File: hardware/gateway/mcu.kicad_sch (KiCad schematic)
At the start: 23 parts, among them IC1 ATTINY406-MFR, J1 M20-9770342, J2 M20-9770342, Q1 IRLML6402TRPBF, U1 2462

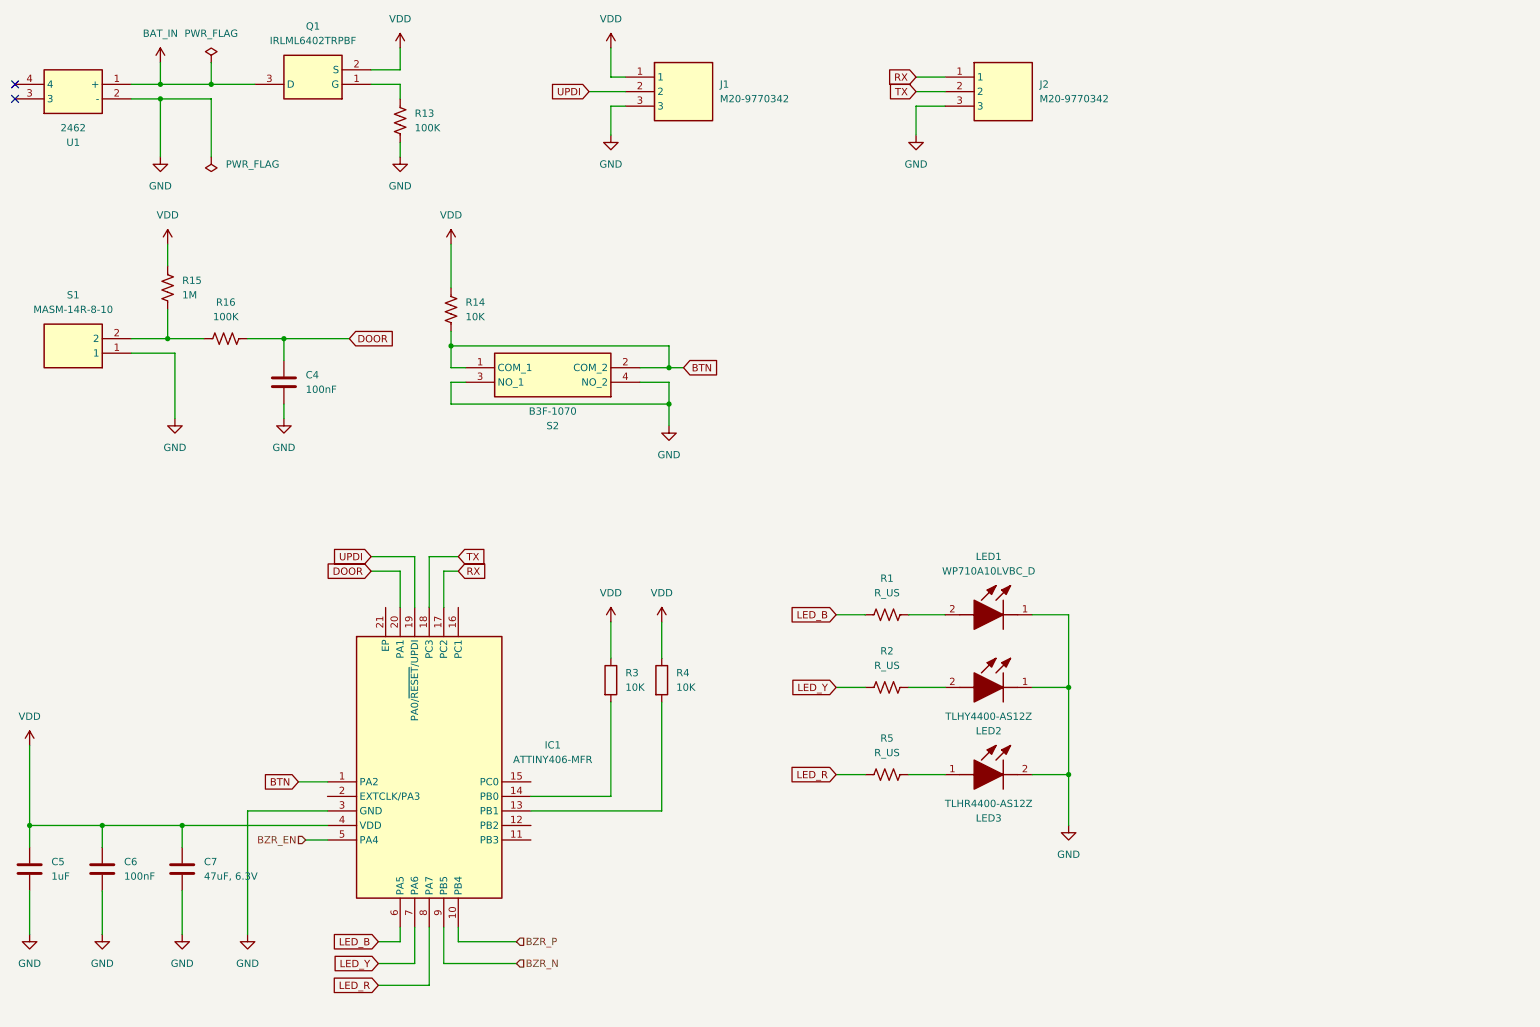
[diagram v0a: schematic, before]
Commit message: EG-11 All components connected in all sheets. The MCU pin mapping needs to be fixed. The BOM needs to be created. The FRAM need needs to be assessed.
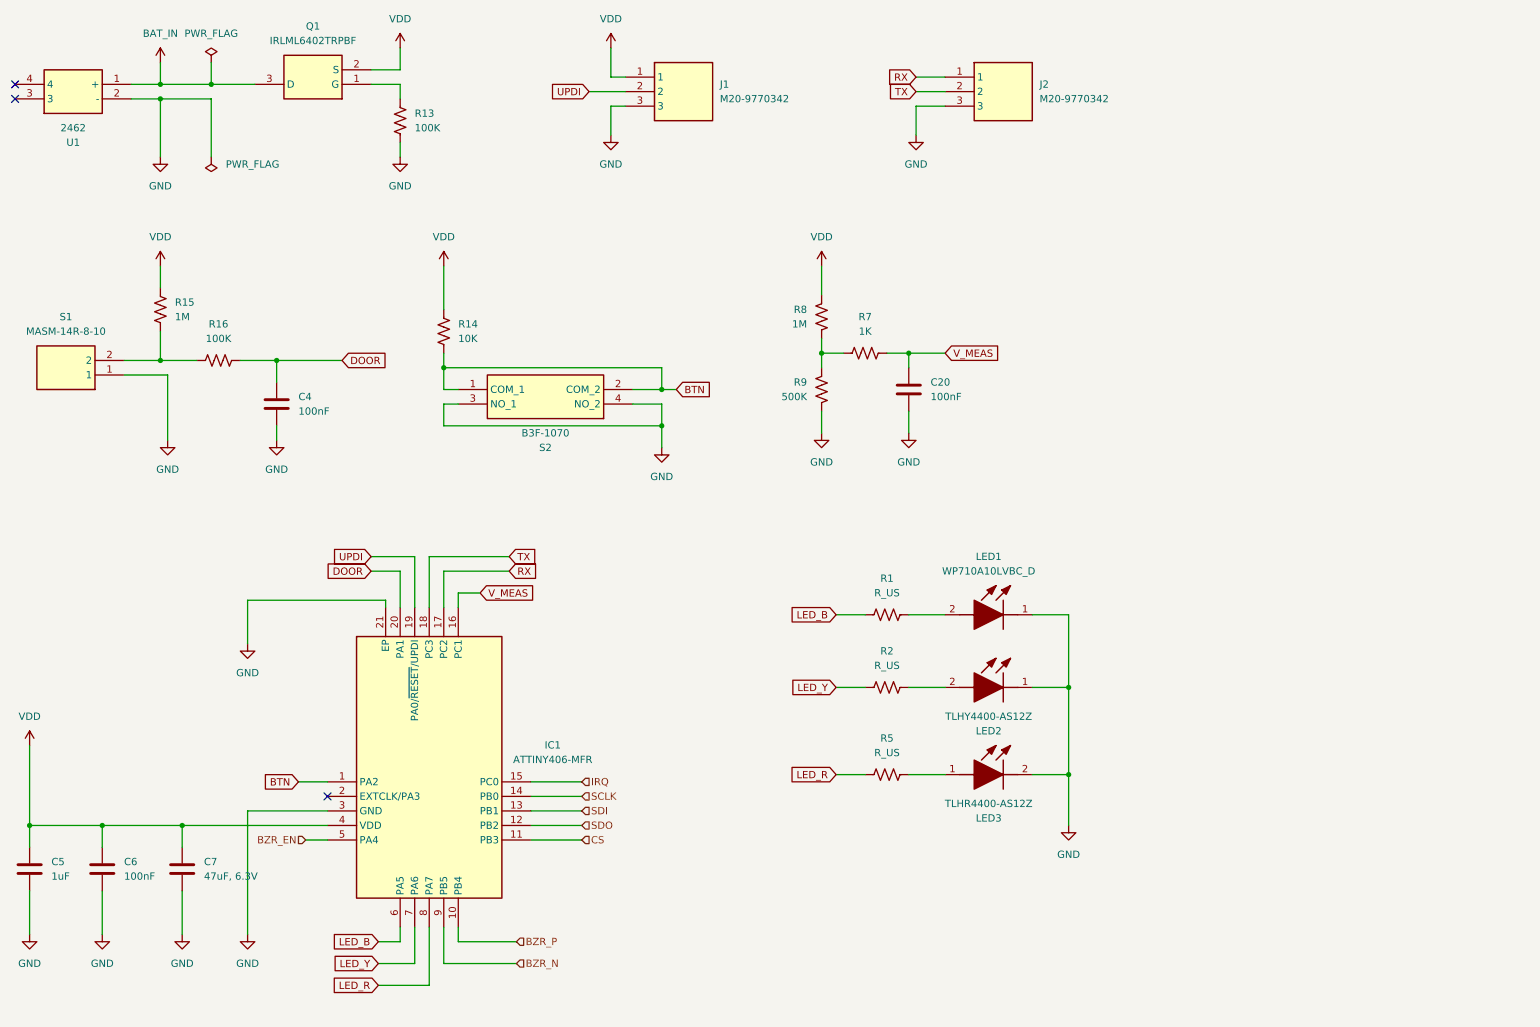
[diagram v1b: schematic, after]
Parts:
- removed R3, R4: 10K, Resistor_SMD:R_0603_1608Metric, symbol Device:R
- added C20: 100nF, Capacitor_SMD:C_0603_1608Metric, symbol Device:C
- added R7: 1K, symbol Device:R_US
- added R8: 1M, symbol Device:R_US
- added R9: 500K, symbol Device:R_US
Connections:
- net GND: now also IC1.21 (EP), C20.2, R9.1
- net VDD: now also R8.2
- net SDI: now reaches IC1.13 (PB1)
- net SCLK: now reaches IC1.14 (PB0)
- net CS: now reaches IC1.11 (PB3)
- net SDO: now reaches IC1.12 (PB2)
- net IRQ: now reaches IC1.15 (PC0)
- net V_MEAS: now reaches IC1.16 (PC1)
- net V_MEAS: now also C20.1, R7.2
- new net: R7.1, R8.1, R9.2
- no-connect marks 2 -> 3
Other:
- moved on the sheet: C4, R14, R15, R16, S1, S2

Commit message: EG-11 FRAM included, MCU pin mapping finished. Only BOM is not finished.
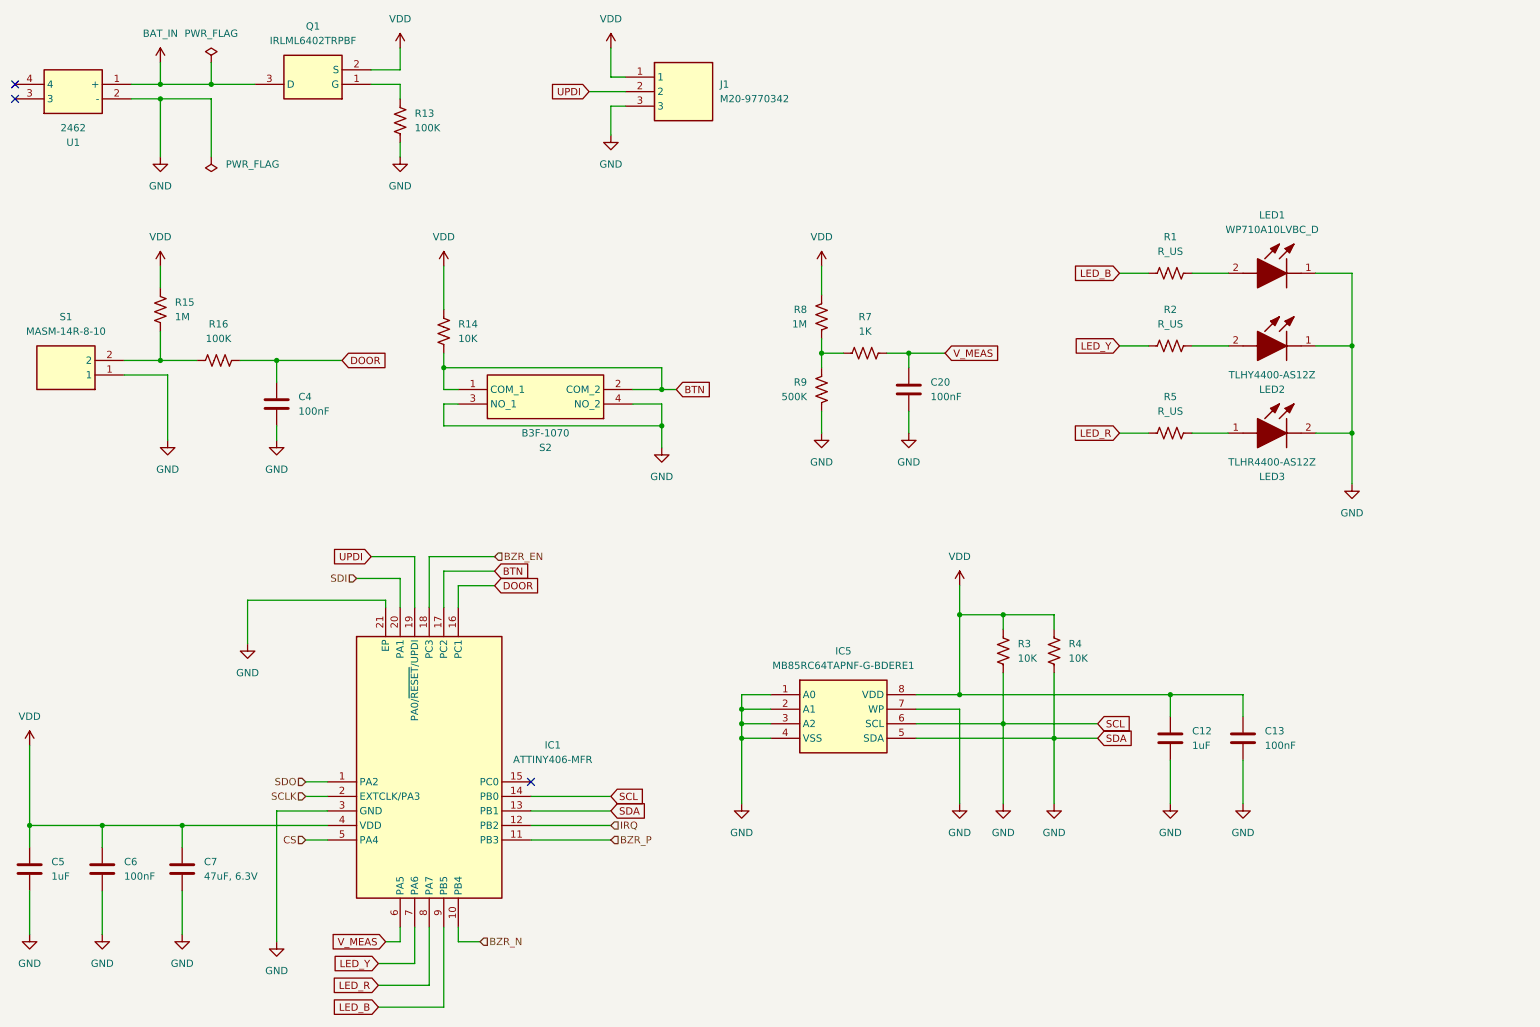
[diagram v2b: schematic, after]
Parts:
- removed J2: M20-9770342, MyParts:HDRV3W66P0X254_1X3_762X254X855P, symbol M20-9770342:M20-9770342
- added C12: 1uF, Capacitor_SMD:C_0603_1608Metric, symbol Device:C
- added C13: 100nF, Capacitor_SMD:C_0603_1608Metric, symbol Device:C
- added IC5: MB85RC64TAPNF-G-BDERE1, MyParts:SOIC127P602X173-8N, symbol MB85RC64TAPNF-G-BDERE1:MB85RC64TAPNF-G-BDERE1
- added R3, R4: 10K, symbol Device:R_US
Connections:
- net RX is gone; now on net BTN: IC1.17 (PC2)
- net TX is gone; now on net BZR_EN: IC1.18 (PC3)
- net BTN: no longer IC1.1 (PA2)
- net BZR_EN: no longer IC1.5 (PA4)
- net BZR_N: now also IC1.10 (PB4); no longer IC1.9 (PB5)
- net BZR_P: now also IC1.11 (PB3); no longer IC1.10 (PB4)
- net CS: now also IC1.5 (PA4); no longer IC1.11 (PB3)
- net DOOR: now also IC1.16 (PC1); no longer IC1.20 (PA1)
- net GND: now also IC1.13 (PB1), IC1.14 (PB0), C12.2, C13.2, IC5.1 (A0), IC5.2 (A1), IC5.3 (A2), IC5.4 (VSS), IC5.5 (SDA), IC5.6 (SCL), IC5.7 (WP), R3.2, R4.2
- net IRQ: now also IC1.12 (PB2); no longer IC1.15 (PC0)
- net LED_B: now also IC1.9 (PB5); no longer IC1.6 (PA5)
- net SCLK: now also IC1.2 (EXTCLK/PA3); no longer IC1.14 (PB0)
- net SDI: now also IC1.20 (PA1); no longer IC1.13 (PB1)
- net SDO: now also IC1.1 (PA2); no longer IC1.12 (PB2)
- net VDD: now also C12.1, C13.1, IC5.8 (VDD), R3.1, R4.1
- net V_MEAS: now also IC1.6 (PA5); no longer IC1.16 (PC1)
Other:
- moved on the sheet: LED1, LED2, LED3, R1, R2, R5

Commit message: EG-11 Changed the MCU from ATtiny to STML8 due to minimum supply voltage.
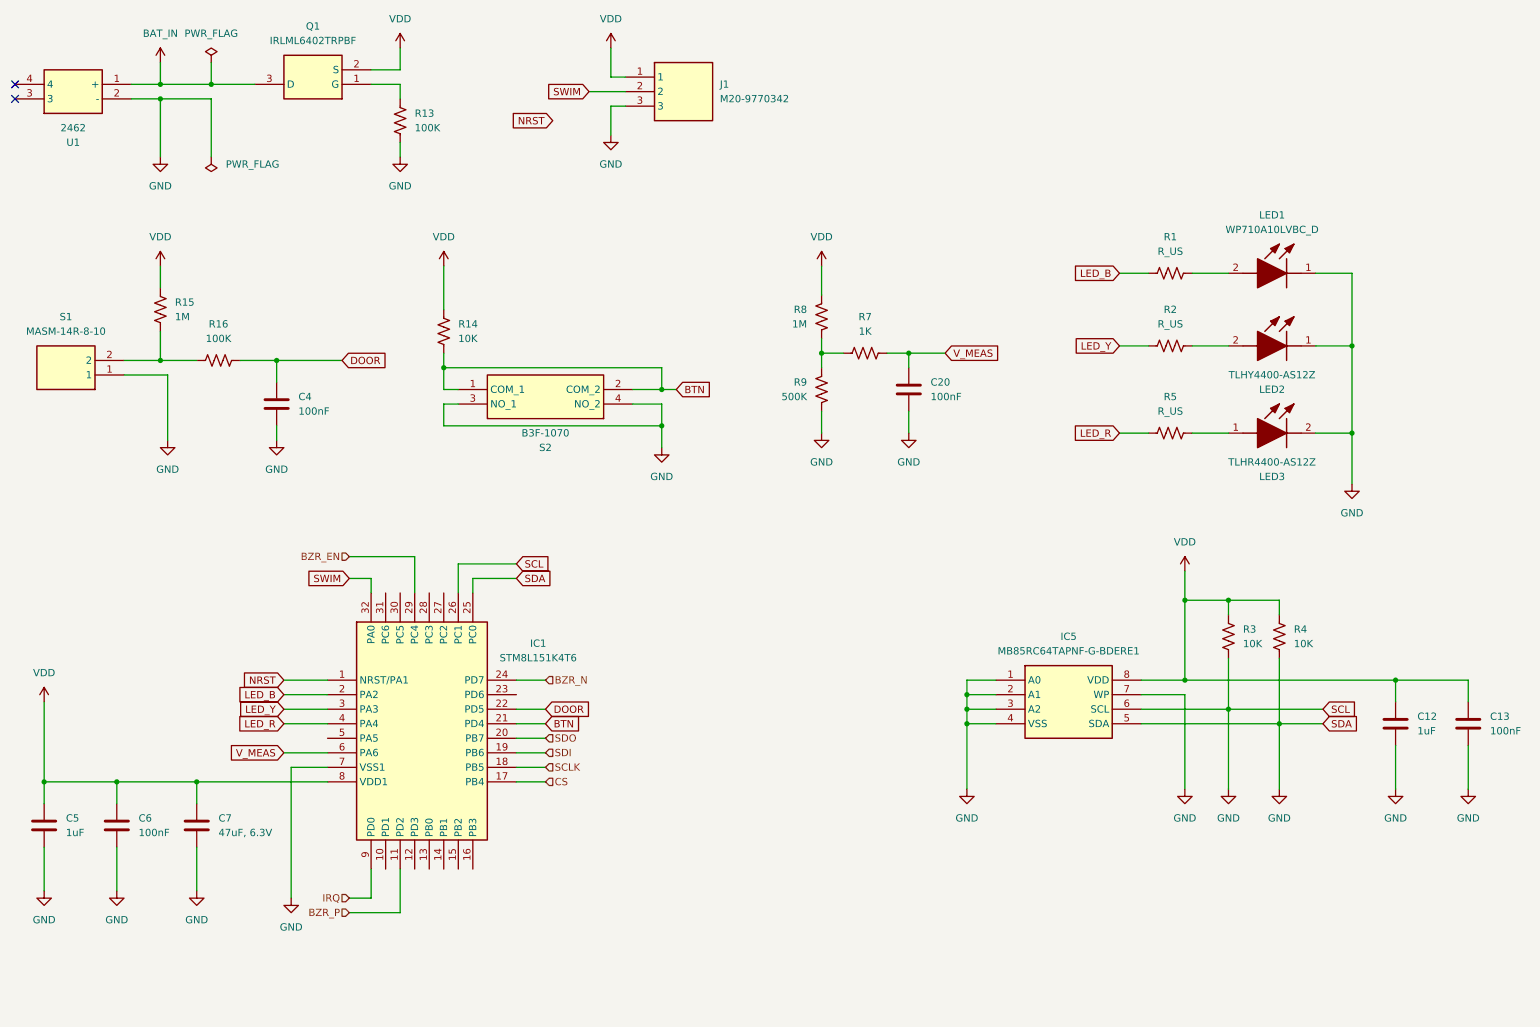
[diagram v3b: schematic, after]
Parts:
- removed IC1: ATTINY406-MFR, MyParts:QFN40P300X300X90-21N, symbol ATTINY406-MFR:ATTINY406-MFR
- added IC1: STM8L151K4T6, MyParts:QFP80P900X900X160-32N, symbol STM8L151K4T6:STM8L151K4T6
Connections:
- net BTN: now also IC1.21 (PD4)
- net BZR_EN: now also IC1.29 (PC4)
- net BZR_N: now also IC1.24 (PD7)
- net BZR_P: now also IC1.11 (PD2)
- net CS: now also IC1.17 (PB4)
- net DOOR: now also IC1.22 (PD5)
- net GND: now also IC1.25 (PC0), IC1.26 (PC1), IC1.7 (VSS1)
- net IRQ: now also IC1.9 (PD0)
- net LED_B: now also IC1.2 (PA2)
- net LED_R: now also IC1.4 (PA4)
- net LED_Y: now also IC1.3 (PA3)
- net SCLK: now also IC1.18 (PB5)
- net SDI: now also IC1.19 (PB6)
- net SDO: now also IC1.20 (PB7)
- net VDD: now also IC1.8 (VDD1)
- net V_MEAS: now also IC1.6 (PA6)
- net UPDI renamed SWIM
- net SWIM: now also IC1.32 (PA0)
- new net NRST: IC1.1 (NRST/PA1)
- no-connect marks 3 -> 2
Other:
- moved on the sheet: C12, C13, C5, C6, C7, IC5, R3, R4

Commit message: EG-11 All connections finished. BOM not created yet.
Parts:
- added C14: 10nF, Capacitor_SMD:C_0603_1608Metric, symbol Device:C
- added J2: G8250041000YEU, MyParts:HDRV4W55P0X200_1X4_800X200X635P, symbol G8250041000YEU:G8250041000YEU
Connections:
- net GND: now also C14.2, J2.4
- net NRST: now also C14.1, J2.3
- net SWIM: now also J2.2; no longer J1.2
- net VDD: now also J2.1; no longer J1.1
- net RX: now reaches IC1.27 (PC2)
- net RX: now also J1.2
- net TX: now reaches IC1.28 (PC3)
- net TX: now also J1.1
- no-connect marks 2 -> 12
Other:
- moved on the sheet: C12, C13, IC5, J1, R3, R4

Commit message: EG-11 BOM generated.
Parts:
- removed R1: R_US, symbol Device:R_US
- removed R14: 10K, symbol Device:R_US
- removed R15: 1M, symbol Device:R_US
- removed R16: 100K, symbol Device:R_US
- added R10: 50, Resistor_SMD:R_0402_1005Metric, symbol Device:R_US
- added R11, R12: 10K, Resistor_SMD:R_0402_1005Metric, symbol Device:R_US
- added R6: 510K, Resistor_SMD:R_0402_1005Metric, symbol Device:R_US
- C3: renamed from C14; footprint Capacitor_SMD:C_0603_1608Metric -> Capacitor_SMD:C_0402_1005Metric; Manufacturer_Part_Number GCJ188R72A104KA1D -> GXT155R71C103KE01D; Mouser Part Number 81-GCJ188R72A104KA1D -> 81-GXT155R71C103KE1D; Mouser Price/Stock https://pt.mouser.com/ProductDetail/Murata-Electronics/GCJ1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 -> https://pt.mouser.com/ProductDetail/Murata-Electronics/GXT1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
- R1: renamed from R13; footprint (none) -> Resistor_SMD:R_0402_1005Metric; Manufacturer_Name (none) -> Yageo; Manufacturer_Part_Number (none) -> RC0402JR-7D100KL; Mouser Part Number (none) -> 603-RC0402JR-7D100KL; Mouser Price/Stock (none) -> https://pt.mouser.com/ProductDetail/YAGEO/RC0402JR-7D100KL?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
- R2: value R_US -> 1M; footprint (none) -> Resistor_SMD:R_0402_1005Metric; Manufacturer_Name (none) -> Yageo; Manufacturer_Part_Number (none) -> RC0402JR-7D1ML; Mouser Part Number (none) -> 603-RC0402JR-7D1ML; Mouser Price/Stock (none) -> https://pt.mouser.com/ProductDetail/YAGEO/RC0402JR-7D1ML?qs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
- R3: value 10K -> 100K; footprint (none) -> Resistor_SMD:R_0402_1005Metric; Manufacturer_Name (none) -> Yageo; Manufacturer_Part_Number (none) -> RC0402JR-7D100KL; Mouser Part Number (none) -> 603-RC0402JR-7D100KL; Mouser Price/Stock (none) -> https://pt.mouser.com/ProductDetail/YAGEO/RC0402JR-7D100KL?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
- R4: footprint (none) -> Resistor_SMD:R_0402_1005Metric; Manufacturer_Name (none) -> Panasonic; Manufacturer_Part_Number (none) -> AC0402JR-7D10KL; Mouser Part Number (none) -> 603-AC0402JR-7D10KL; Mouser Price/Stock (none) -> https://pt.mouser.com/ProductDetail/YAGEO/AC0402JR-7D10KL?q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
- R5: value R_US -> 1M; footprint (none) -> Resistor_SMD:R_0402_1005Metric; Manufacturer_Name (none) -> Panasonic; Manufacturer_Part_Number (none) -> ERJ-2RKD1004X; Mouser Part Number (none) -> 667-ERJ-2RKD1004X; Mouser Price/Stock (none) -> https://pt.mouser.com/ProductDetail/Panasonic/ERJ-2RKD1004X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
- R7: footprint (none) -> Resistor_SMD:R_0402_1005Metric; Manufacturer_Name (none) -> Yageo; Manufacturer_Part_Number (none) -> RC0402JR-7D1KL; Mouser Part Number (none) -> 603-RC0402JR-7D1KL; Mouser Price/Stock (none) -> https://pt.mouser.com/ProductDetail/YAGEO/RC0402JR-7D1KL?qs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
- R8: value 1M -> 100; footprint (none) -> Resistor_SMD:R_0402_1005Metric; Manufacturer_Name (none) -> Yageo; Manufacturer_Part_Number (none) -> AC0402JR-7D100RL; Mouser Part Number (none) -> 603-AC0402JR-7D100RL; Mouser Price/Stock (none) -> https://pt.mouser.com/ProductDetail/YAGEO/AC0402JR-7D100RL?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
- R9: value 500K -> 50; footprint (none) -> Resistor_SMD:R_0402_1005Metric; Manufacturer_Name (none) -> Yageo; Manufacturer_Part_Number (none) -> AC0402JR-0750RL; Mouser Part Number (none) -> 603-AC0402JR-0750RL; Mouser Price/Stock (none) -> https://pt.mouser.com/ProductDetail/YAGEO/AC0402JR-0750RL?q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
- renumbered C4 to C1, C20 to C2, C5 to C4, C6 to C5, C7 to C6, C12 to C7, C13 to C8, J2 to J1, J1 to J2
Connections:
- net BTN: now also R4.1
- net DOOR: now also R3.2
- net GND: now also R11.1, R12.1, R6.1; no longer R3.2, R4.2, R9.1
- net LED_B: now also R8.1
- net LED_R: now also R10.1; no longer R5.1
- net LED_Y: now also R9.1; no longer R2.1
- net VDD: now also R2.2, R4.2, R5.2, R11.2, R12.2; no longer R3.1, R4.1, R8.2
- net at LED1.2 (A): now also R8.2
- net at LED3.1 (A): now also R10.2; no longer R5.2
- net at LED2.2 (A): now also R9.2; no longer R2.2
- net at S1.2: now also R2.1, R3.1
- new net: R5.1, R6.2, R7.1
